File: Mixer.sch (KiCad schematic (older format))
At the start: 20 parts

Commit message: Initial layout in PCBNew
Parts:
- C101, C102: renamed from C?; value C -> 47p; footprint (none) -> Capacitor_THT:C_Disc_D3.0mm_W2.0mm_P2.50mm
- J101, J102, J103, J104: renamed from J?; footprint (none) -> A-2563:A-2563
- J105: renamed from J?; footprint (none) -> Connector_PinHeader_2.54mm:PinHeader_2x05_P2.54mm_Vertical
- R101, R102, R103, R104, R105, R107: renamed from R?; value R_US -> 100k; footprint (none) -> Resistor_THT:R_Axial_DIN0207_L6.3mm_D2.5mm_P7.62mm_Horizontal
- R106: renamed from R?; value R_US -> 330; footprint (none) -> Resistor_THT:R_Axial_DIN0207_L6.3mm_D2.5mm_P7.62mm_Horizontal
- RV101, RV102, RV103: renamed from RV?; value R_POT_US -> 100k; footprint (none) -> A-5513:A-5513
- U101: renamed from U?; footprint (none) -> Package_DIP:DIP-8_W7.62mm
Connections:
- net GND: now also J102.S, J103.S, RV101.1, RV102.1, RV103.1; no longer RV101.3, RV102.3, RV103.3
- net at J101.T: now also RV102.3; no longer RV102.1
- net at J102.T: now also RV103.3; no longer RV103.1
- net at J103.T: now also RV101.3; no longer RV101.1

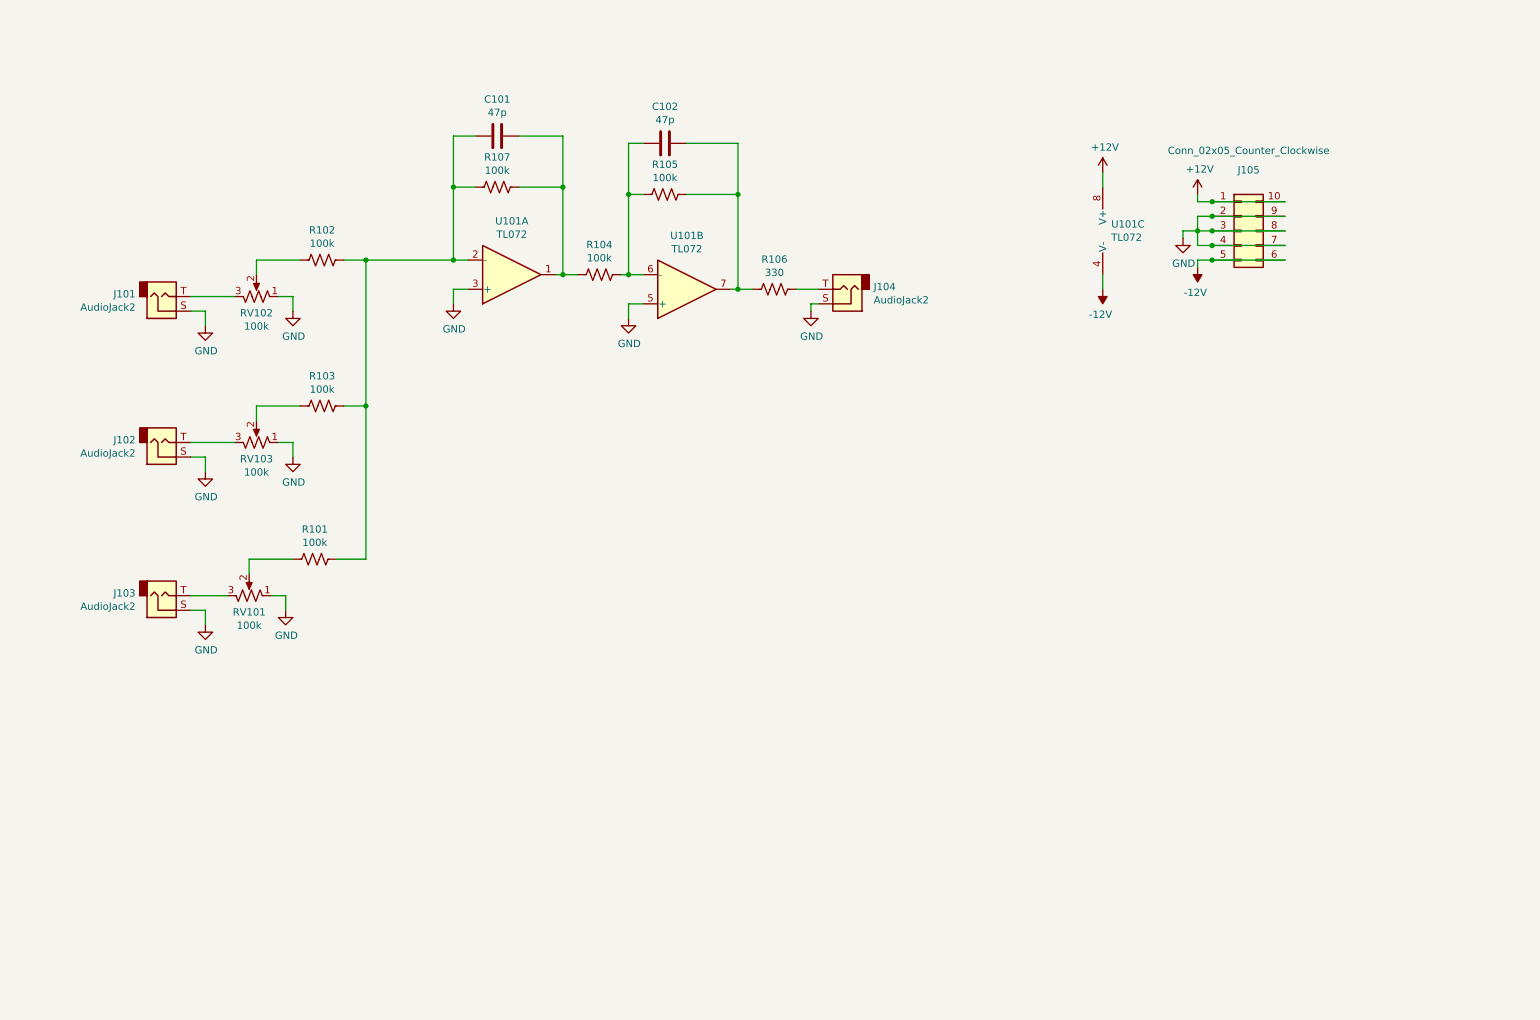
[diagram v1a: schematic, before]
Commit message: Added attenuverters
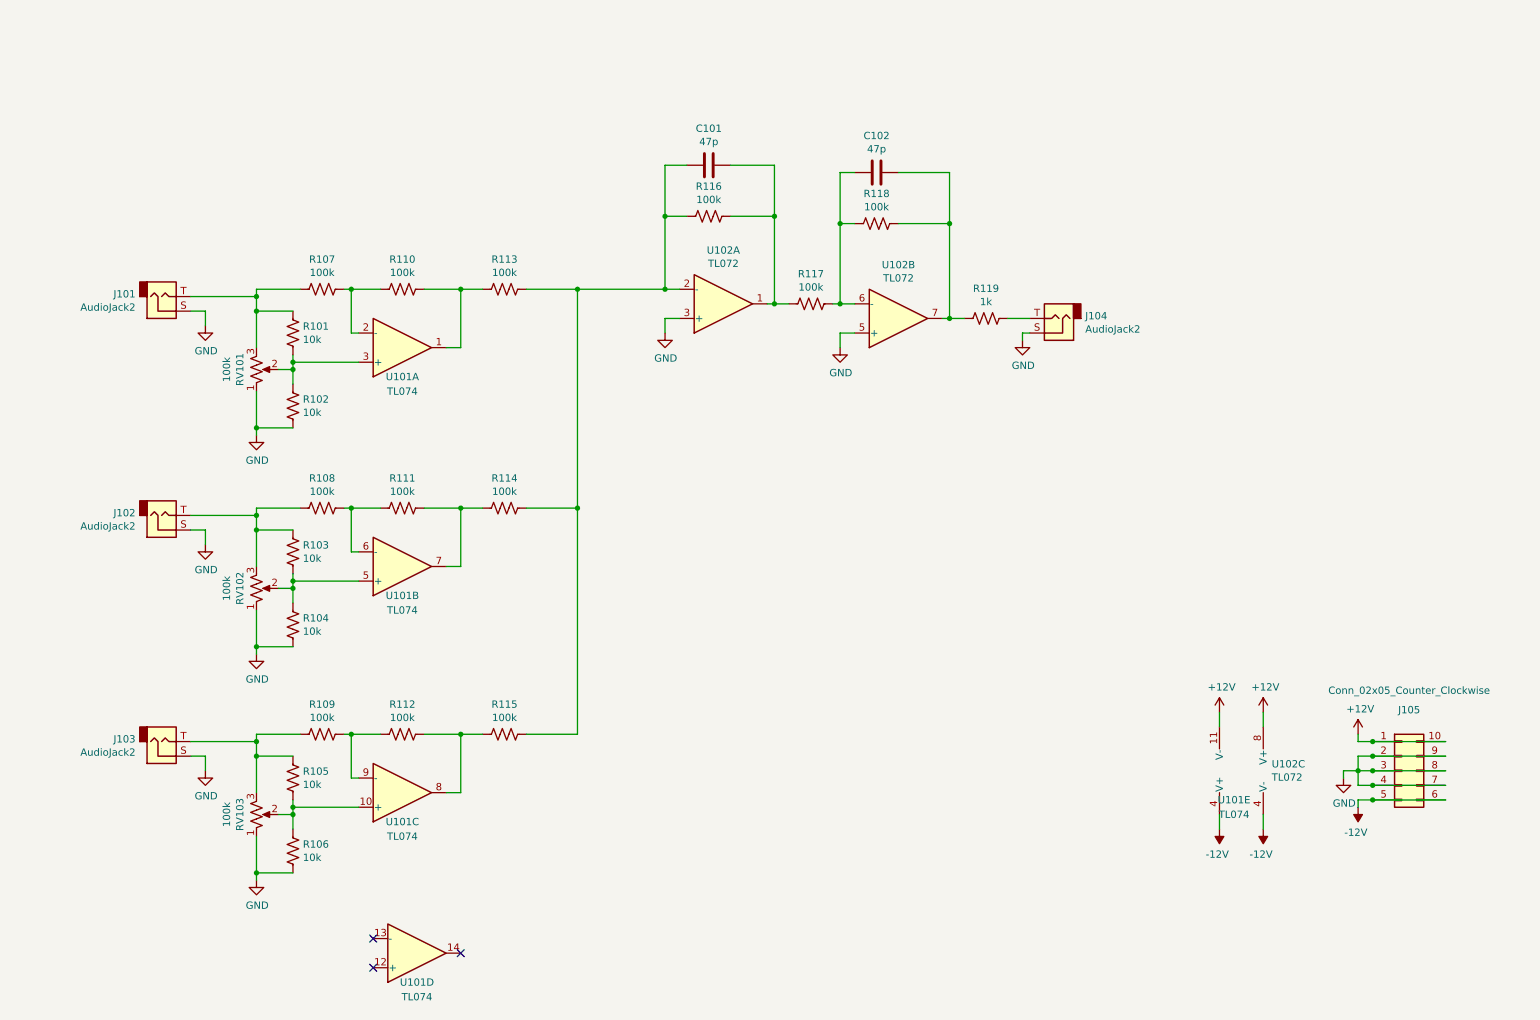
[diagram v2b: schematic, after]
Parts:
- removed RV101: 100k, A-5513:A-5513, symbol Device:R_POT_US
- added R102, R104, R105, R106: 10k, Resistor_THT:R_Axial_DIN0207_L6.3mm_D2.5mm_P7.62mm_Horizontal, symbol Device:R_US
- added R108, R109, R110, R111, R112, R113, R114, R115: 100k, Resistor_THT:R_Axial_DIN0207_L6.3mm_D2.5mm_P7.62mm_Horizontal, symbol Device:R_US
- added RV102: 100k, A-5513:A-5513, symbol Device:R_POT_US
- added U101: TL074, Package_DIP:DIP-14_W7.62mm, symbol Amplifier_Operational:TL074
- R101, R103: value 100k -> 10k
- R119: renamed from R106; value 330 -> 1k
- renumbered R102 to R107, R107 to R116, R104 to R117, R105 to R118, RV102 to RV101, U101 to U102
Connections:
- net +12V: now also U101.11 (V-)
- net -12V: now also U101.4 (V+)
- net GND: now also R102.2, R104.2, R106.2, RV102.1
- net at J101.T, RV101.3: now also R101.1, R107.2
- net at RV101.2: now also R101.2, R102.1, U101.3 (+); no longer R107.2
- net at C101.2, R116.2, U102.2 (-): now also R113.1, R114.1, R115.1; no longer R101.1, R103.1, R107.1
- net at J102.T: now also R103.1, R108.2, RV102.3; no longer RV103.3
- net at J103.T: now also RV103.3, R105.1, R109.2
- net at R103.2: now also R104.1, RV102.2, U101.5 (+); no longer RV103.2
- new net: R107.1, R110.2, U101.2 (-)
- new net: R110.1, R113.2, U101.1
- new net: R108.1, R111.2, U101.6 (-)
- new net: R111.1, R114.2, U101.7
- new net: R105.2, R106.1, RV103.2, U101.10 (+)
- new net: R109.1, R112.2, U101.9 (-)
- new net: R112.1, R115.2, U101.8
- no-connect marks 0 -> 3
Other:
- moved on the sheet: C101, C102, J104, J105, R107, R116, R117, R118, R119, RV101, U102A, U102B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

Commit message: 47pF caps and 100k resistors converted to SMD
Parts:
- C101, C102: footprint Capacitor_THT:C_Disc_D3.0mm_W2.0mm_P2.50mm -> Capacitor_SMD:C_0402_1005Metric; LCSC (none) -> C1567
- R107, R108, R109, R110, R111, R112, R113, R114, R115, R116, R117, R118: footprint Resistor_THT:R_Axial_DIN0207_L6.3mm_D2.5mm_P7.62mm_Horizontal -> Resistor_SMD:R_0805_2012Metric; LCSC (none) -> C17407
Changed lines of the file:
@@
 F 0 "R107" V 3045 2400 50  0000 C CNN
 F 1 "100k" V 3136 2400 50  0000 C CNN
-F 2 "Resistor_THT:R_Axial_DIN0207_L6.3mm_D2.5mm_P7.62mm_Horizontal" V 3290 2390 50  0001 C CNN
+F 2 "Resistor_SMD:R_0805_2012Metric" V 3290 2390 50  0001 C CNN
 F 3 "~" H 3250 2400 50  0001 C CNN
+F 4 "C17407" V 3250 2400 50  0001 C CNN "LCSC"
 	1    3250 2400
 	0    1    1    0
@@
 F 0 "C101" V 5648 1550 50  0000 C CNN
 F 1 "47p" V 5739 1550 50  0000 C CNN
-F 2 "Capacitor_THT:C_Disc_D3.0mm_W2.0mm_P2.50mm" H 5938 1400 50  0001 C CNN
+F 2 "Capacitor_SMD:C_0402_1005Metric" H 5938 1400 50  0001 C CNN
 F 3 "~" H 5900 1550 50  0001 C CNN
+F 4 "C1567" V 5900 1550 50  0001 C CNN "LCSC"
 	1    5900 1550
 	0    1    1    0
@@
 F 0 "R116" V 5695 1900 50  0000 C CNN
 F 1 "100k" V 5786 1900 50  0000 C CNN
-F 2 "Resistor_THT:R_Axial_DIN0207_L6.3mm_D2.5mm_P7.62mm_Horizontal" V 5940 1890 50  0001 C CNN
+F 2 "Resistor_SMD:R_0805_2012Metric" V 5940 1890 50  0001 C CNN
 F 3 "~" H 5900 1900 50  0001 C CNN
+F 4 "C17407" V 5900 1900 50  0001 C CNN "LCSC"
 	1    5900 1900
 	0    1    1    0
@@
 F 0 "R117" V 6395 2500 50  0000 C CNN
 F 1 "100k" V 6486 2500 50  0000 C CNN
-F 2 "Resistor_THT:R_Axial_DIN0207_L6.3mm_D2.5mm_P7.62mm_Horizontal" V 6640 2490 50  0001 C CNN
+F 2 "Resistor_SMD:R_0805_2012Metric" V 6640 2490 50  0001 C CNN
 F 3 "~" H 6600 2500 50  0001 C CNN
+F 4 "C17407" V 6600 2500 50  0001 C CNN "LCSC"
 	1    6600 2500
 	0    1    1    0
@@
 F 0 "C102" V 6798 1600 50  0000 C CNN
 F 1 "47p" V 6889 1600 50  0000 C CNN
-F 2 "Capacitor_THT:C_Disc_D3.0mm_W2.0mm_P2.50mm" H 7088 1450 50  0001 C CNN
+F 2 "Capacitor_SMD:C_0402_1005Metric" H 7088 1450 50  0001 C CNN
 F 3 "~" H 7050 1600 50  0001 C CNN
+F 4 "C1567" V 7050 1600 50  0001 C CNN "LCSC"
 	1    7050 1600
 	0    1    1    0
@@
 F 0 "R118" V 6845 1950 50  0000 C CNN
 F 1 "100k" V 6936 1950 50  0000 C CNN
-F 2 "Resistor_THT:R_Axial_DIN0207_L6.3mm_D2.5mm_P7.62mm_Horizontal" V 7090 1940 50  0001 C CNN
+F 2 "Resistor_SMD:R_0805_2012Metric" V 7090 1940 50  0001 C CNN
 F 3 "~" H 7050 1950 50  0001 C CNN
+F 4 "C17407" V 7050 1950 50  0001 C CNN "LCSC"
 	1    7050 1950
 	0    1    1    0
@@
 F 0 "R110" V 3595 2400 50  0000 C CNN
 F 1 "100k" V 3686 2400 50  0000 C CNN
-F 2 "Resistor_THT:R_Axial_DIN0207_L6.3mm_D2.5mm_P7.62mm_Horizontal" V 3840 2390 50  0001 C CNN
+F 2 "Resistor_SMD:R_0805_2012Metric" V 3840 2390 50  0001 C CNN
 F 3 "~" H 3800 2400 50  0001 C CNN
+F 4 "C17407" V 3800 2400 50  0001 C CNN "LCSC"
 	1    3800 2400
 	0    1    1    0
@@
 F 0 "R108" V 3045 3900 50  0000 C CNN
 F 1 "100k" V 3136 3900 50  0000 C CNN
-F 2 "Resistor_THT:R_Axial_DIN0207_L6.3mm_D2.5mm_P7.62mm_Horizontal" V 3290 3890 50  0001 C CNN
+F 2 "Resistor_SMD:R_0805_2012Metric" V 3290 3890 50  0001 C CNN
 F 3 "~" H 3250 3900 50  0001 C CNN
+F 4 "C17407" V 3250 3900 50  0001 C CNN "LCSC"
 	1    3250 3900
 	0    1    1    0
@@
 F 0 "R111" V 3595 3900 50  0000 C CNN
 F 1 "100k" V 3686 3900 50  0000 C CNN
-F 2 "Resistor_THT:R_Axial_DIN0207_L6.3mm_D2.5mm_P7.62mm_Horizontal" V 3840 3890 50  0001 C CNN
+F 2 "Resistor_SMD:R_0805_2012Metric" V 3840 3890 50  0001 C CNN
 F 3 "~" H 3800 3900 50  0001 C CNN
+F 4 "C17407" V 3800 3900 50  0001 C CNN "LCSC"
 	1    3800 3900
 	0    1    1    0
@@
 F 0 "R109" V 3045 5450 50  0000 C CNN
 F 1 "100k" V 3136 5450 50  0000 C CNN
-F 2 "Resistor_THT:R_Axial_DIN0207_L6.3mm_D2.5mm_P7.62mm_Horizontal" V 3290 5440 50  0001 C CNN
+F 2 "Resistor_SMD:R_0805_2012Metric" V 3290 5440 50  0001 C CNN
 F 3 "~" H 3250 5450 50  0001 C CNN
+F 4 "C17407" V 3250 5450 50  0001 C CNN "LCSC"
 	1    3250 5450
 	0    1    1    0
@@
 F 0 "R112" V 3595 5450 50  0000 C CNN
 F 1 "100k" V 3686 5450 50  0000 C CNN
-F 2 "Resistor_THT:R_Axial_DIN0207_L6.3mm_D2.5mm_P7.62mm_Horizontal" V 3840 5440 50  0001 C CNN
+F 2 "Resistor_SMD:R_0805_2012Metric" V 3840 5440 50  0001 C CNN
 F 3 "~" H 3800 5450 50  0001 C CNN
+F 4 "C17407" V 3800 5450 50  0001 C CNN "LCSC"
 	1    3800 5450
 	0    1    1    0
@@
 F 0 "R113" V 4295 2400 50  0000 C CNN
 F 1 "100k" V 4386 2400 50  0000 C CNN
-F 2 "Resistor_THT:R_Axial_DIN0207_L6.3mm_D2.5mm_P7.62mm_Horizontal" V 4540 2390 50  0001 C CNN
+F 2 "Resistor_SMD:R_0805_2012Metric" V 4540 2390 50  0001 C CNN
 F 3 "~" H 4500 2400 50  0001 C CNN
+F 4 "C17407" V 4500 2400 50  0001 C CNN "LCSC"
 	1    4500 2400
 	0    1    1    0
@@
 F 0 "R114" V 4295 3900 50  0000 C CNN
 F 1 "100k" V 4386 3900 50  0000 C CNN
-F 2 "Resistor_THT:R_Axial_DIN0207_L6.3mm_D2.5mm_P7.62mm_Horizontal" V 4540 3890 50  0001 C CNN
+F 2 "Resistor_SMD:R_0805_2012Metric" V 4540 3890 50  0001 C CNN
 F 3 "~" H 4500 3900 50  0001 C CNN
+F 4 "C17407" V 4500 3900 50  0001 C CNN "LCSC"
 	1    4500 3900
 	0    1    1    0
@@
 F 0 "R115" V 4295 5450 50  0000 C CNN
 F 1 "100k" V 4386 5450 50  0000 C CNN
-F 2 "Resistor_THT:R_Axial_DIN0207_L6.3mm_D2.5mm_P7.62mm_Horizontal" V 4540 5440 50  0001 C CNN
+F 2 "Resistor_SMD:R_0805_2012Metric" V 4540 5440 50  0001 C CNN
 F 3 "~" H 4500 5450 50  0001 C CNN
+F 4 "C17407" V 4500 5450 50  0001 C CNN "LCSC"
 	1    4500 5450
 	0    1    1    0
